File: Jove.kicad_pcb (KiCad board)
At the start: 2 copper layers, 65 x 100 mm, 156 parts, among them J1 PJ301B, J2 PJ301B, J3 PJ301B, J4 PJ301B, J5 PJ301B, J6 PJ301B, P1 CONN_02X05, Q1 BCM857BS, Q2 BCM857BS, Q3 J112, Q4 J112, Q5 J112, Q6 J112, SW1 KS-01Q, U1 TL072-, U10 CD4027, U11 CD40106, U12 TS321, U13 TS321, U2 TL072-, U3 TL072-, U4 TL072-, U5 LM13700, U6 LM13700, U7 LM13700, U8 DG409, U9 CD4052

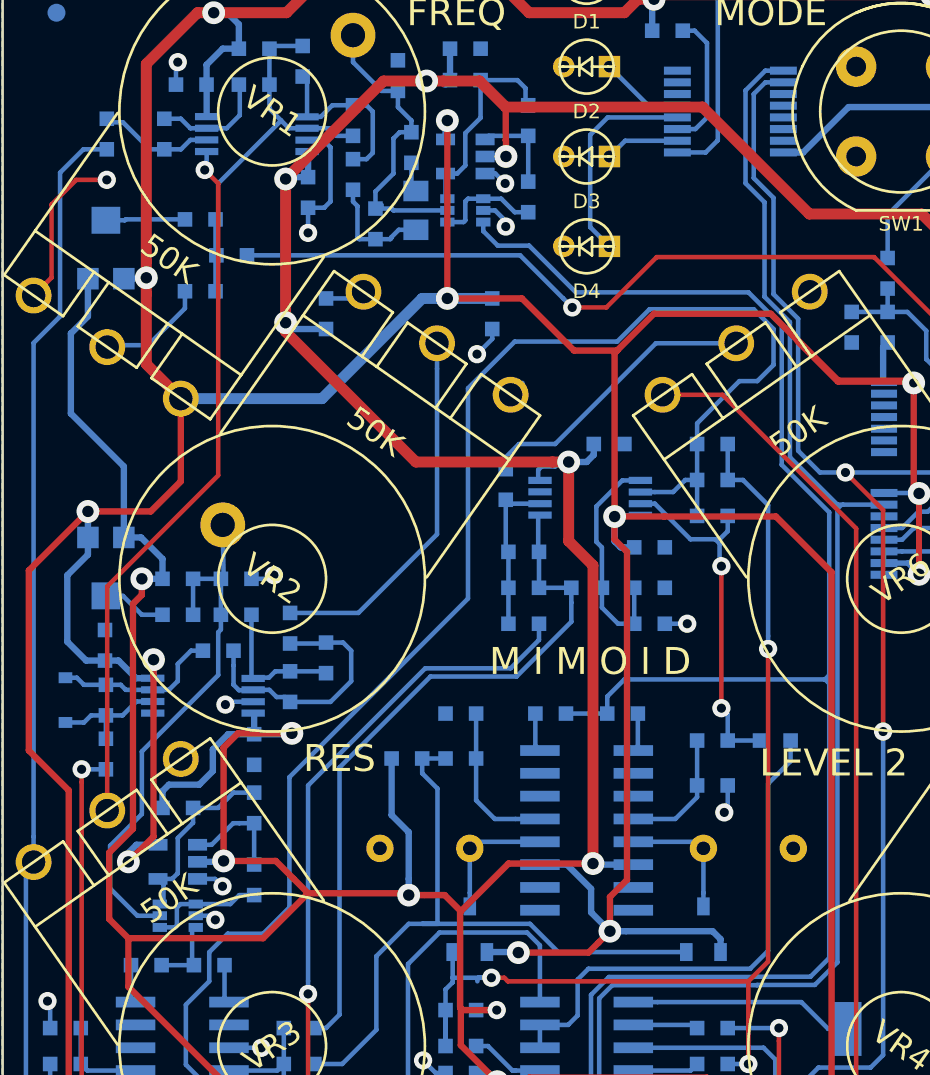
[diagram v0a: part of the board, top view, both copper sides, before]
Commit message: changed BCM857BS SOT-363 to BCM857BV SOT-666
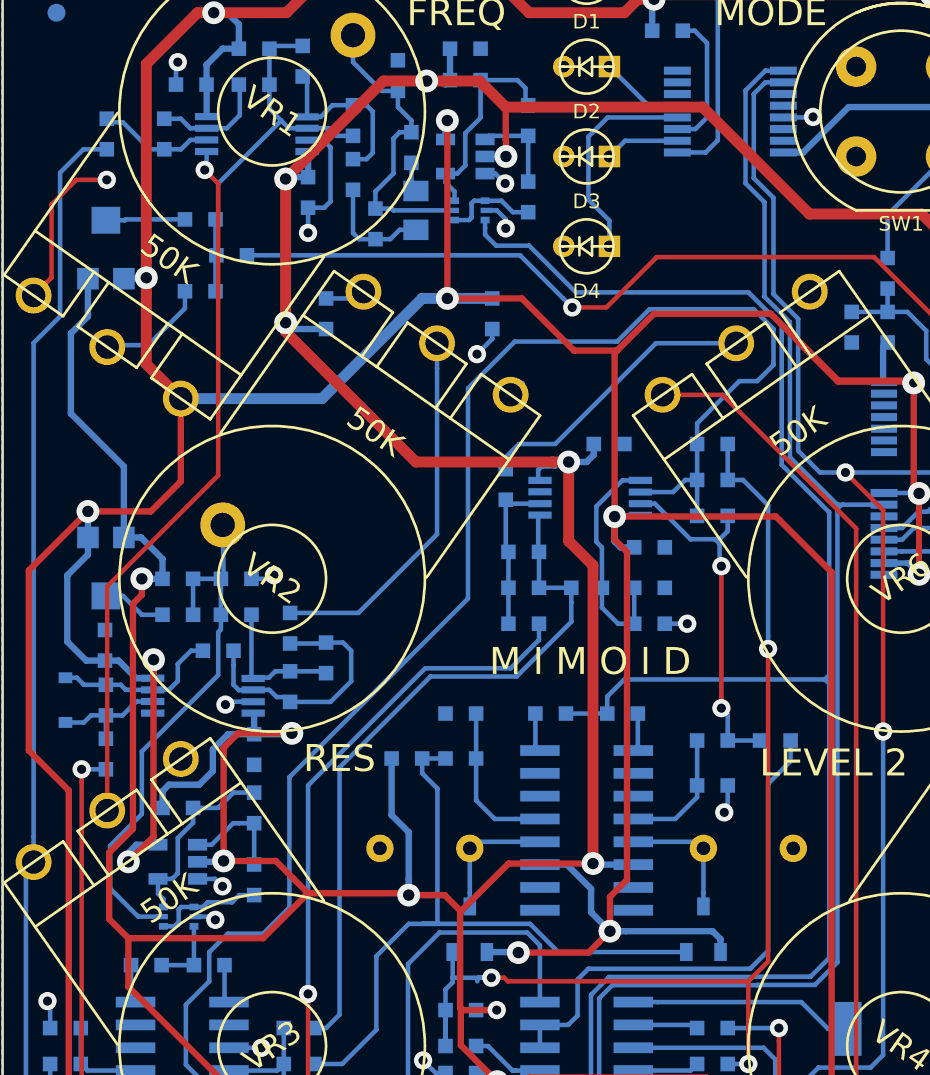
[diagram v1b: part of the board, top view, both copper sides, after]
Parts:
- Q1, Q2: footprint SMD TRAN:sot323-6 -> TO_SOT_Packages_SMD:SOT-666
- moved Q2 0.25 mm to (38.0, 26.0), turned to 180 degrees
- moved Q1 0.07 mm to (21.8, 65.3), turned to 180 degrees
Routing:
- net GND: track 45.8 -> 47.4 mm, vias 19 -> 20
- net Net-(Q2-Pad1): track 5.97 -> 5.28 mm
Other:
- rule pad_to_mask_clearance: 0 -> 0.025
- board text added: "DIY JOVE"
- board text added: "Multimode Filter v1.6 09 2018"
- board text removed: "JOVE"
- board text removed: "Multimode Filter v1.5 11 2017"
